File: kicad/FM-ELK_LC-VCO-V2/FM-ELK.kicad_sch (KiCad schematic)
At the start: 11 parts, among them Q1 BS170, Q2 BS170, Q3 BS170, Q4 BS170

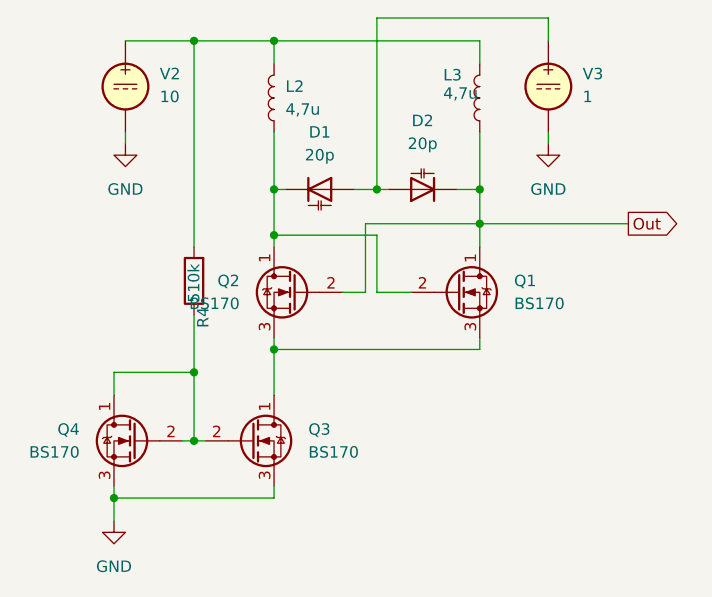
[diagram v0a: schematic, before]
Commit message: Bauteilwerte angepasst und lib hinzugefügt
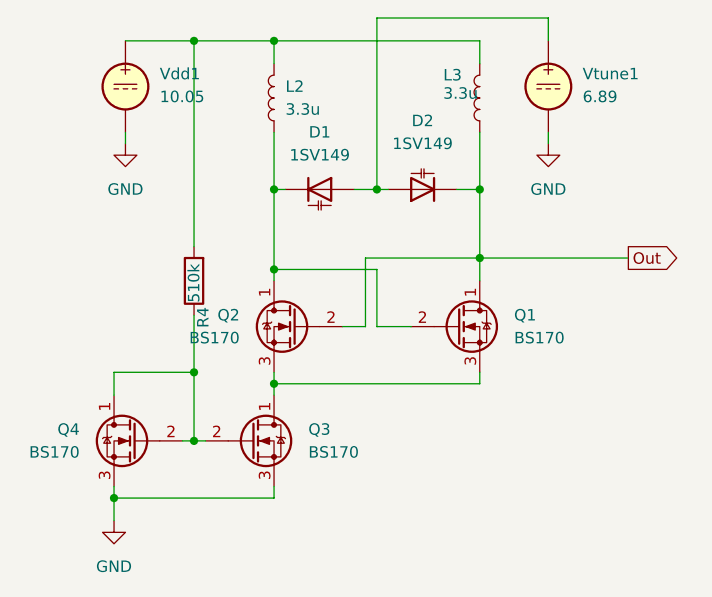
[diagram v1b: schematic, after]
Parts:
- D1, D2: value 20p -> 1SV149
- L2, L3: value 4,7u -> 3.3u
- Vdd1: renamed from V2; value 10 -> 10.05
- Vtune1: renamed from V3; value 1 -> 6.89
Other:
- moved on the sheet: Q1, Q2
